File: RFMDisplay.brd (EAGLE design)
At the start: 86.3 x 102.5 mm, 16 parts, among them IC1 74HCT595N, IC2 74HCT595N, IC3 74HCT595N, IC4 74HCT595N

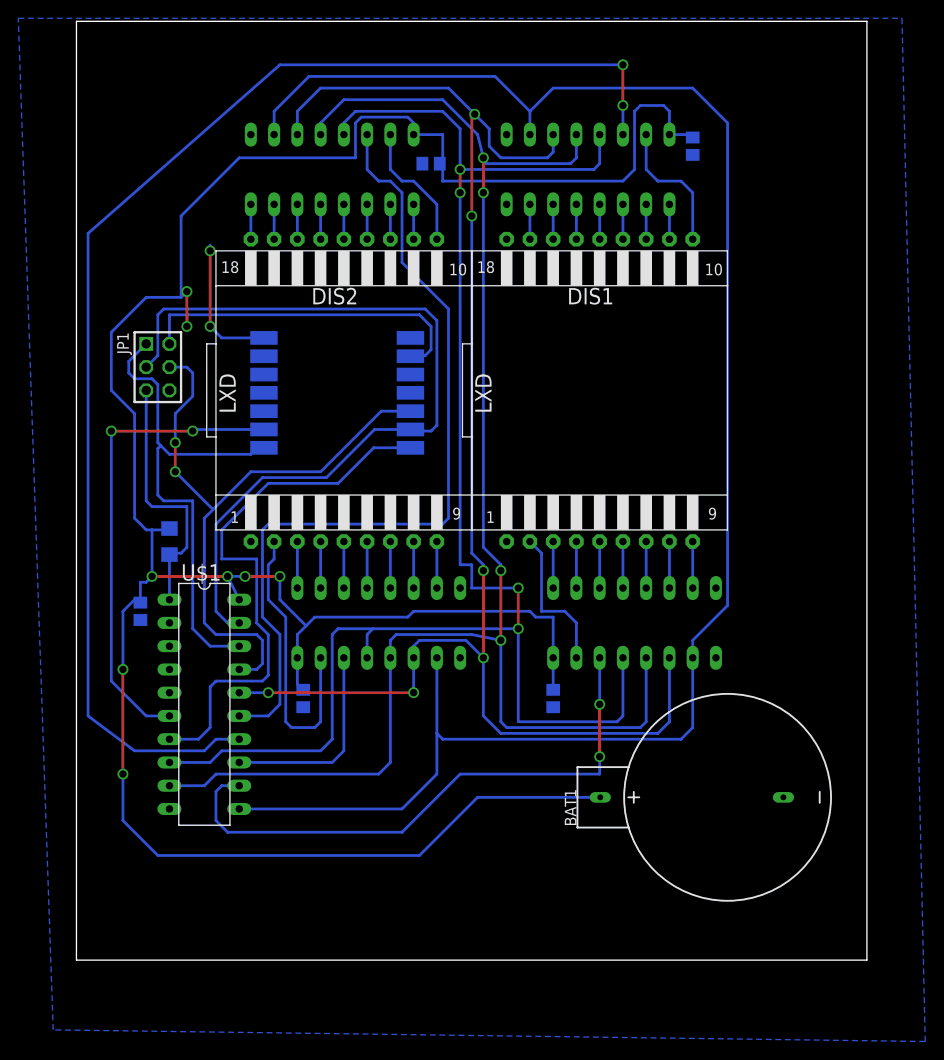
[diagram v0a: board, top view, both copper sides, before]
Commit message: Increased pad size
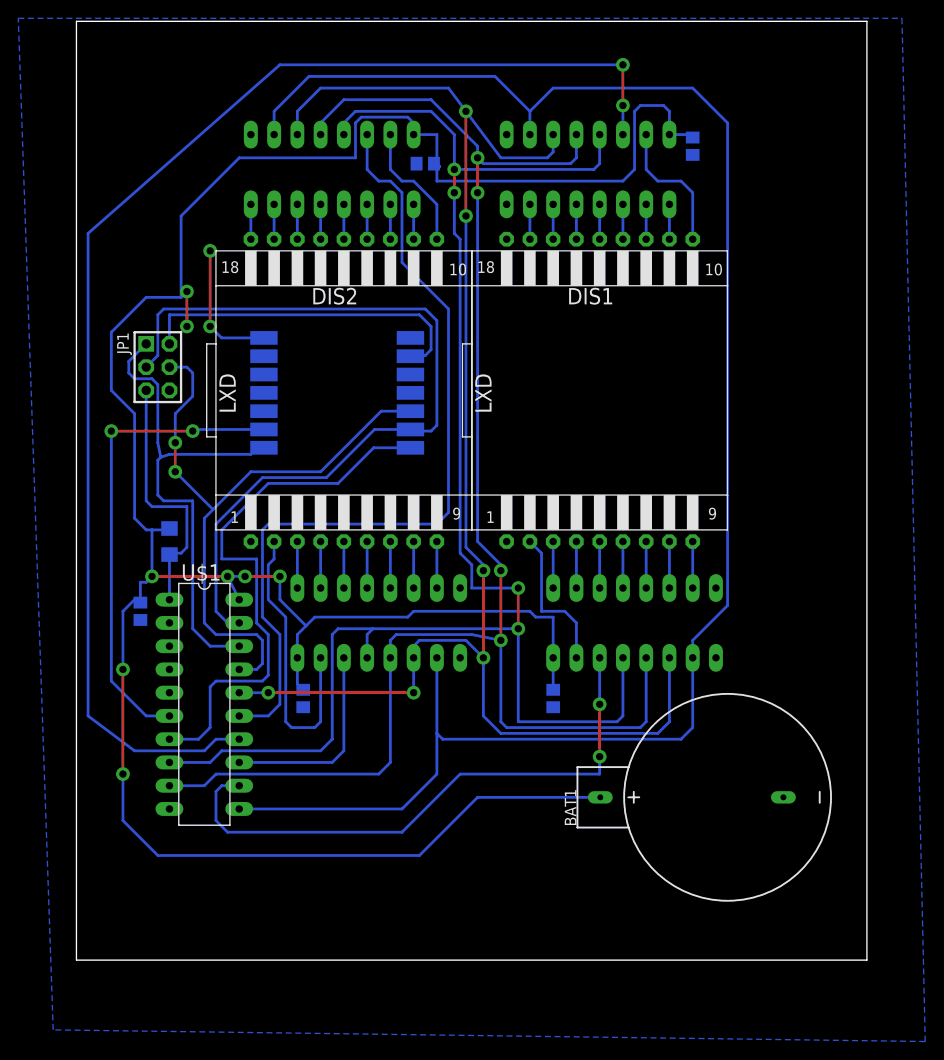
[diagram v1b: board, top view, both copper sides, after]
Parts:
- moved C3 0.63 mm to (38.1, 87.0)
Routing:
- net SR_OE: track 177.4 -> 176.6 mm
- net SR_SCK: track 166.4 -> 165.8 mm

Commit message: Adjusted some wire widths
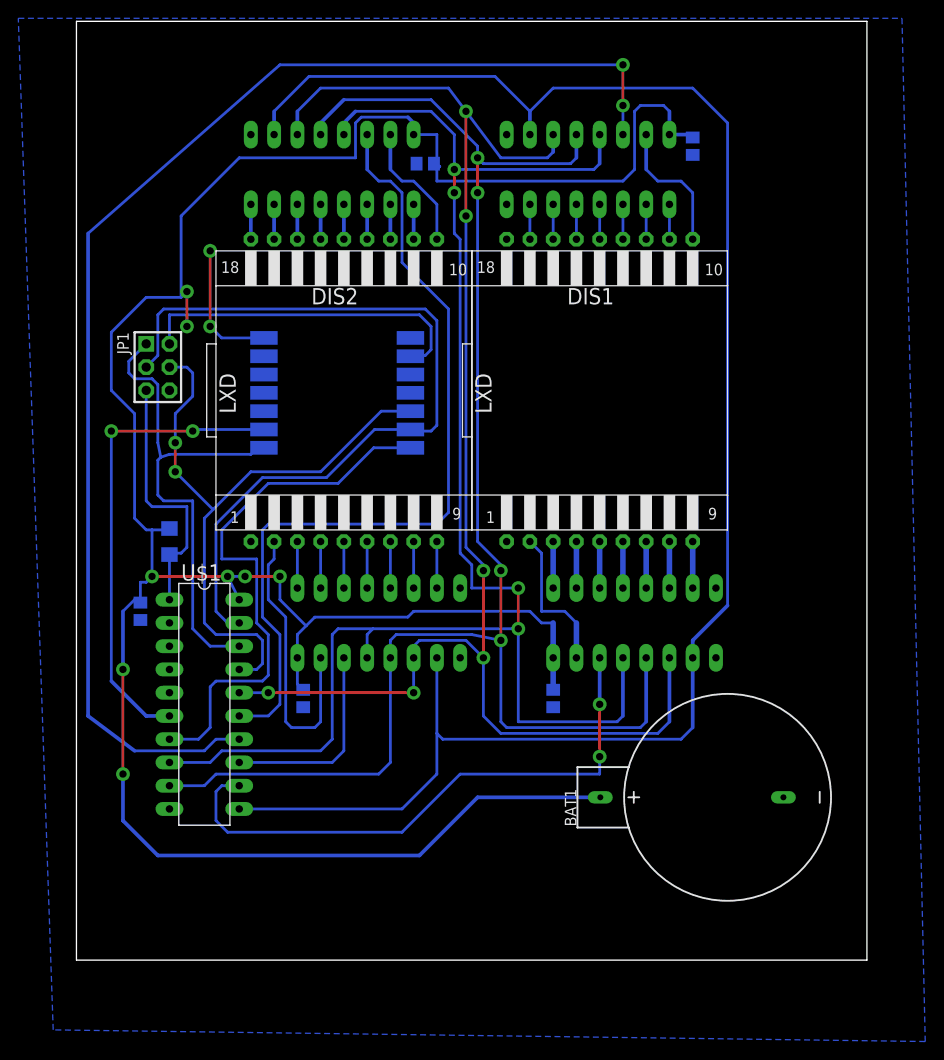
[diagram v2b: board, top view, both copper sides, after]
